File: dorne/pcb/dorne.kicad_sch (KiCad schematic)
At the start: 146 parts, among them J1 MJ-4PP-9, J2 OLED, J3 MJ-4PP-9, J4 OLED, SW1 SW_PUSH, SW10 SW_PUSH, SW11 SW_PUSH, SW12 SW_PUSH, SW13 SW_PUSH, SW14 SW_PUSH, SW15 SW_PUSH, SW16 SW_PUSH, SW17 SW_PUSH, SW18 SW_PUSH, SW19 SW_PUSH, SW2 SW_PUSH, SW20 SW_PUSH, SW21 SW_PUSH, SW22 SW_PUSH, SW23 SW_PUSH, SW24 SW_PUSH, SW25 SW_PUSH, SW26 SW_PUSH, SW27 SW_PUSH, SW28 SW_PUSH, SW29 SW_PUSH, SW3 SW_PUSH, SW30 SW_PUSH, SW31 SW_PUSH, SW32 SW_PUSH, SW33 SW_PUSH, SW34 SW_PUSH, SW35 SW_PUSH, SW36 SW_PUSH, SW37 SW_PUSH, SW38 SW_PUSH, SW39 SW_PUSH, SW4 SW_PUSH, SW40 SW_PUSH, SW41 SW_PUSH, SW42 SW_PUSH, SW5 SW_PUSH, SW6 SW_PUSH, SW7 SW_PUSH, SW8 SW_PUSH, SW9 SW_PUSH, U1 ProMicro, U2 ProMicro

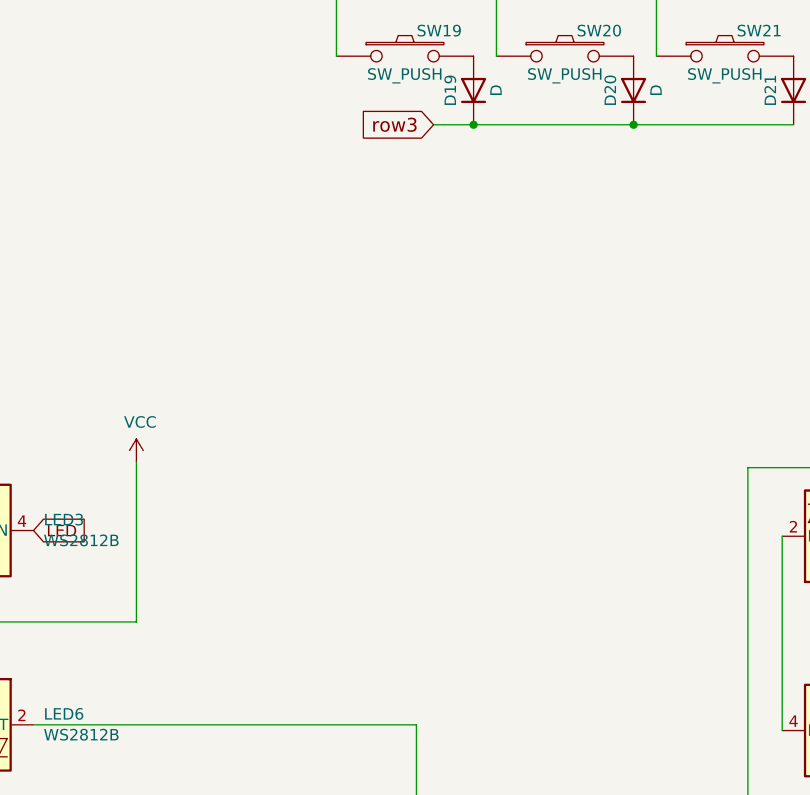
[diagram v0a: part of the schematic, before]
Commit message: Add Nice-Nano
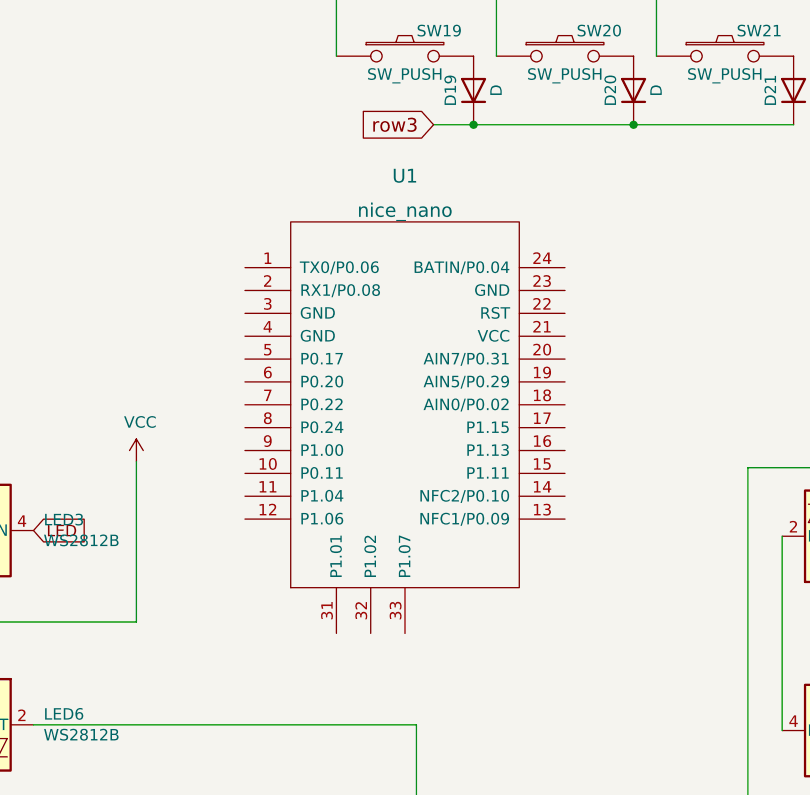
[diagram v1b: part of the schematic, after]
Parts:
- added U1: nice_nano, symbol nice:nice_nano
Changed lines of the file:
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@@
     (pin "1")
+  )
+  (symbol (lib_id "nice:nice_nano") (at 152.4 115.57 0) (unit 1)
+    (in_bom yes) (on_board yes) (fields_autoplaced)
+    (property "Reference" "U1" (id 0) (at 152.4 91.44 0)
+      (effects (font (size 1.524 1.524)))
+    )
+    (property "Value" "nice_nano" (id 1) (at 152.4 95.25 0)
+      (effects (font (size 1.524 1.524)))
+    )
+    (property "Footprint" "" (id 2) (at 179.07 179.07 90)
+      (effects (font (size 1.524 1.524)) hide)
+    )
+    (property "Datasheet" "" (id 3) (at 179.07 179.07 90)
+      (effects (font (size 1.524 1.524)) hide)
+    )
+    (pin "1")
+    (pin "10")
+    (pin "11")
+    (pin "12")
+    (pin "13")
+    (pin "14")
+    (pin "15")
+    (pin "16")
+    (pin "17")
+    (pin "18")
+    (pin "19")
+    (pin "2")
+    (pin "20")
+    (pin "21")
+    (pin "22")
+    (pin "23")
+    (pin "24")
+    (pin "3")
+    (pin "31")
+    (pin "32")
+    (pin "33")
+    (pin "4")
+    (pin "5")
+    (pin "6")
+    (pin "7")
+    (pin "8")
+    (pin "9")
   )
   (sheet_instances
@@
       (reference "U1") (unit 1) (value "ProMicro") (footprint "kbd:ProMicro_v3")
     )
+    (path "/2c564cbd-303f-4000-890a-52bc3be8e7ab"
+      (reference "U1") (unit 1) (value "nice_nano") (footprint "")
+    )
     (path "/00000000-0000-0000-0000-00005c25f857"

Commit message: RM LEDs
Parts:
- removed LED1, LED2, LED28, LED29, LED3, LED30, LED31, LED32, LED33, LED4, LED5, LED6: WS2812B, LED_SMD:LED_WS2812B_PLCC4_5.0x5.0mm_P3.2mm, symbol LED:WS2812B
- removed LED10, LED11, LED12, LED13, LED14, LED15, LED16, LED17, LED18, LED19, LED20, LED21, LED22, LED23, LED24, LED25, LED26, LED27, LED34, LED35, LED36, LED37, LED38, LED39, LED40, LED41, LED42, LED43, LED44, LED45, LED46, LED47, LED48, LED49, LED50, LED51, LED52, LED53, LED54, LED7, LED8, LED9: YS-SK6812MINI-E, kbd:YS-SK6812MINI-E, symbol kbd:YS-SK6812MINI-E
- removed U1: nice_nano, symbol nice:nice_nano
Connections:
- no-connect marks 14 -> 12

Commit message: cherry->choc
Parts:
- SW1, SW10, SW11, SW12, SW13, SW14, SW15, SW16, SW17, SW18, SW19, SW2, SW20, SW22, SW23, SW24, SW25, SW26, SW27, SW28, SW29, SW3, SW30, SW31, SW32, SW33, SW34, SW35, SW36, SW37, SW38, SW39, SW4, SW40, SW41, SW5, SW6, SW7, SW8, SW9: footprint kbd:CherryMX_Hotswap -> kbd:ChocV1_V2_Hotswap
- SW21, SW42: footprint kbd:CherryMX_Hotswap_1.5u -> kbd:ChocV1_V2_Hotswap_1.5u

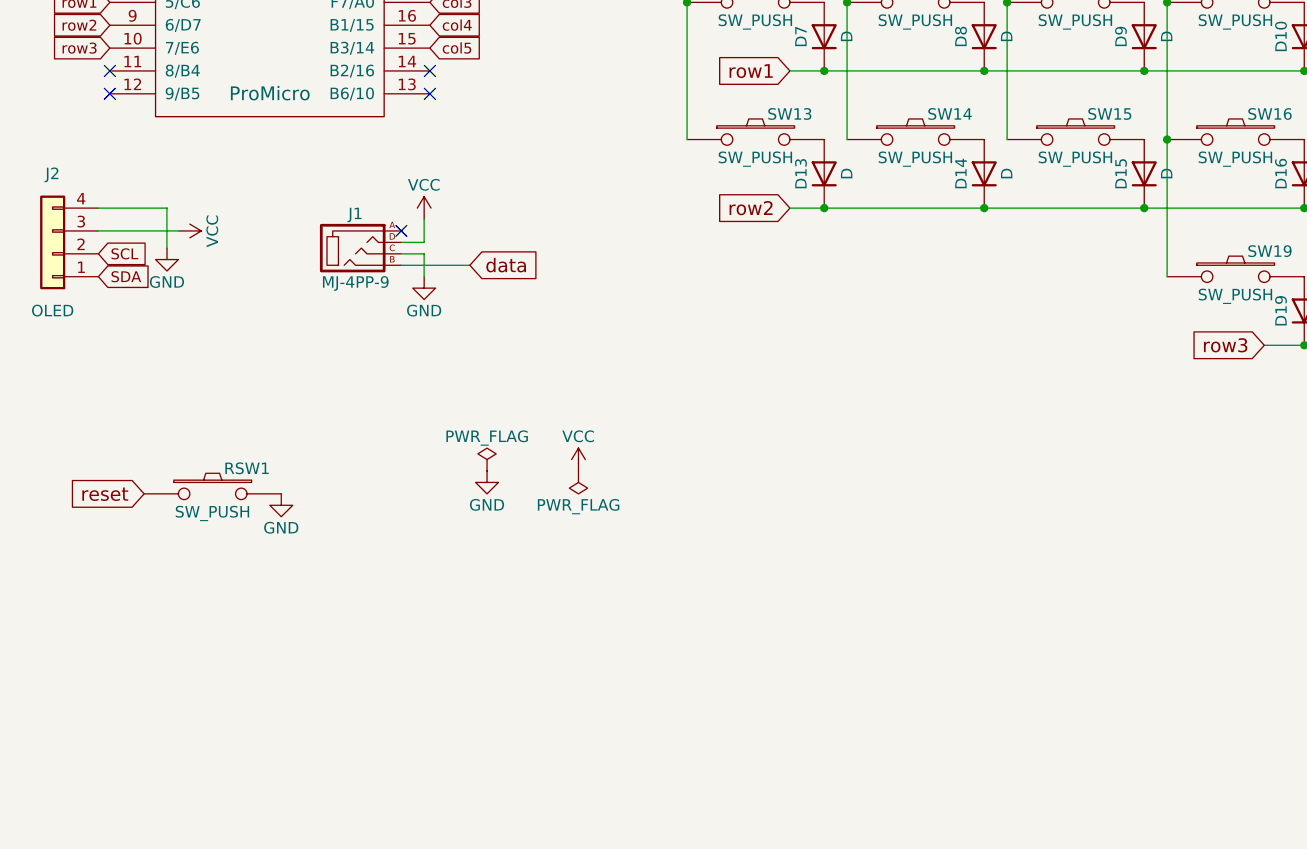
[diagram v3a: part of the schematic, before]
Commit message: Starting to integrate nice nano
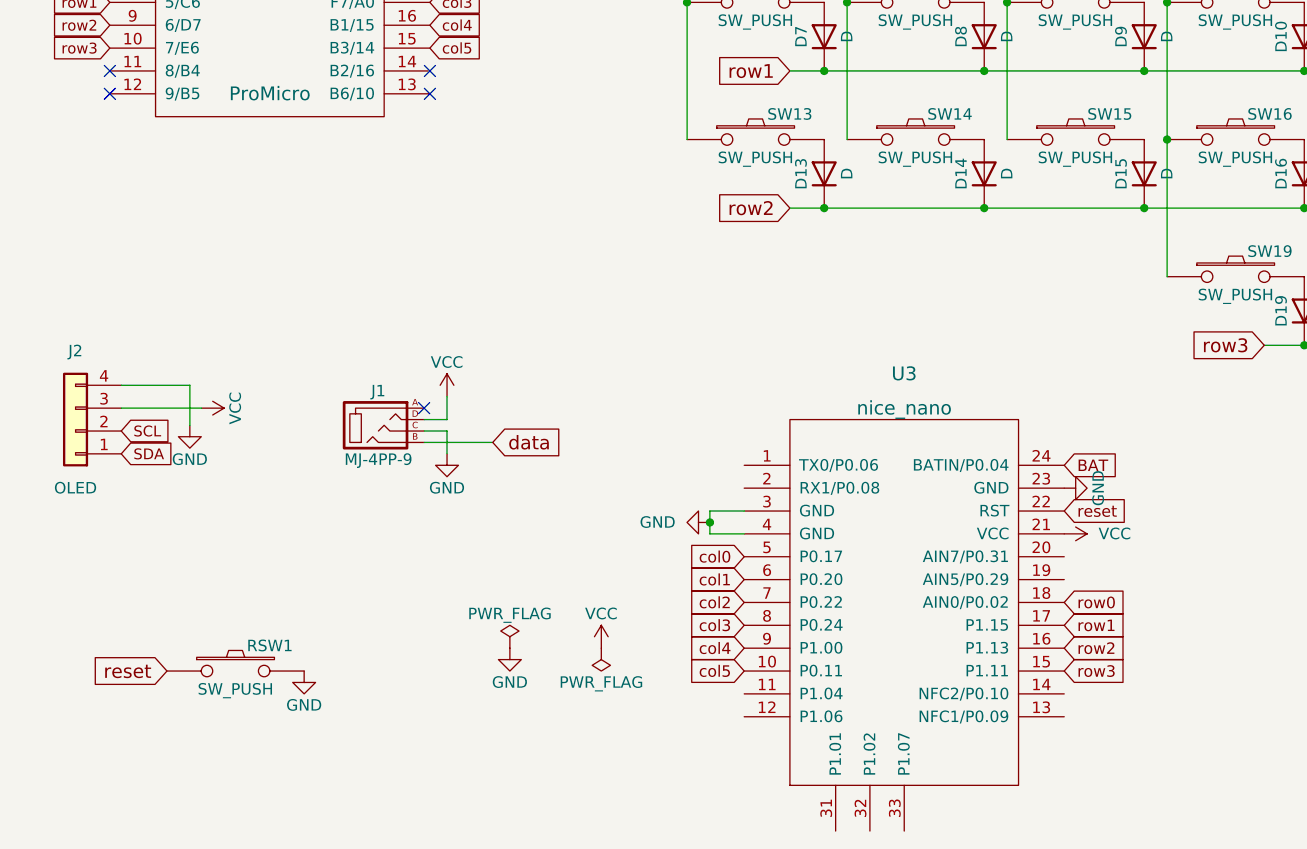
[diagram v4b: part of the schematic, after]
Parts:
- added U3: nice_nano, symbol nice:nice_nano
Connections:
- net GND: now also U3.23 (GND), U3.3 (GND), U3.4 (GND)
- net VCC: now also U3.21 (VCC)
- net col0: now also U3.5 (P0.17)
- net col1: now also U3.6 (P0.20)
- net col2: now also U3.7 (P0.22)
- net col3: now also U3.8 (P0.24)
- net col4: now also U3.9 (P1.00)
- net col5: now also U3.10 (P0.11)
- net reset: now also U3.22 (RST)
- net row0: now also U3.18 (AIN0/P0.02)
- net row1: now also U3.17 (P1.15)
- net row2: now also U3.16 (P1.13)
- net row3: now also U3.15 (P1.11)
- new net BAT: U3.24 (BATIN/P0.04)
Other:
- moved on the sheet: J1, J2, RSW1

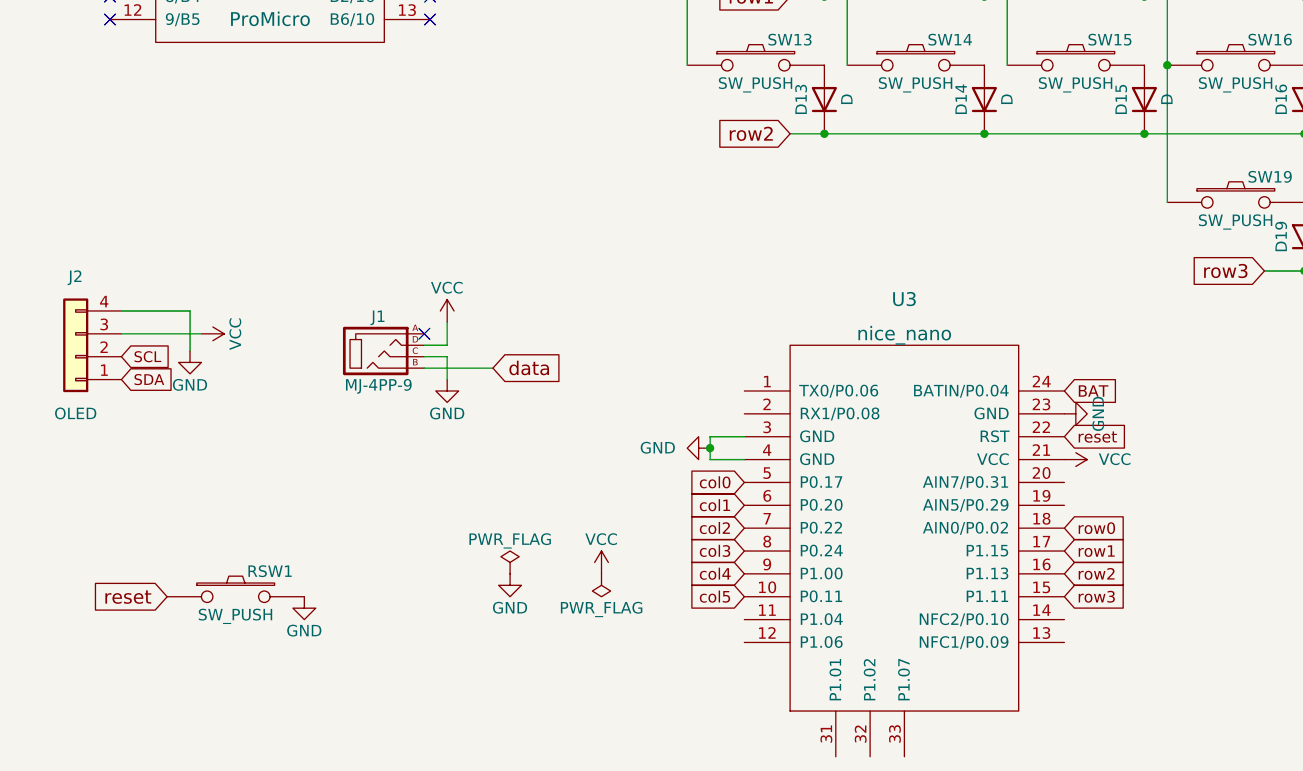
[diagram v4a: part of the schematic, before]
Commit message: Left half is routed better now
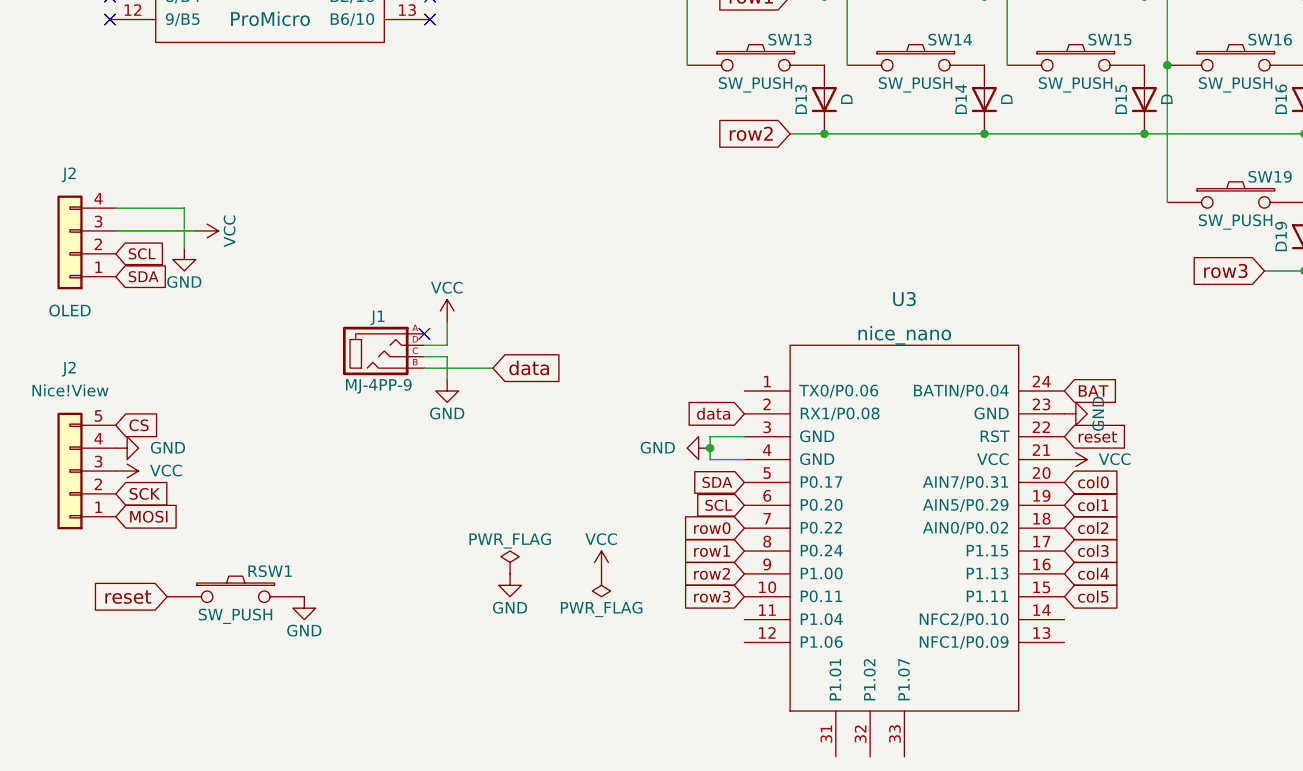
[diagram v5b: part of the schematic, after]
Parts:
- added J2: Nice!View, symbol Connector_Generic:Conn_01x05
- U3: footprint (none) -> nicenano:nice_nano
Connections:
- net GND: now also J2.4 (Pin_4)
- net SCL: now also U3.6 (P0.20)
- net SDA: now also U3.5 (P0.17)
- net VCC: now also J2.3 (Pin_3)
- net col0: now also U3.20 (AIN7/P0.31); no longer U3.5 (P0.17)
- net col1: now also U3.19 (AIN5/P0.29); no longer U3.6 (P0.20)
- net col2: now also U3.18 (AIN0/P0.02); no longer U3.7 (P0.22)
- net col3: now also U3.17 (P1.15); no longer U3.8 (P0.24)
- net col4: now also U3.16 (P1.13); no longer U3.9 (P1.00)
- net col5: now also U3.15 (P1.11); no longer U3.10 (P0.11)
- net data: now also U3.2 (RX1/P0.08)
- net row0: now also U3.7 (P0.22); no longer U3.18 (AIN0/P0.02)
- net row1: now also U3.8 (P0.24); no longer U3.17 (P1.15)
- net row2: now also U3.9 (P1.00); no longer U3.16 (P1.13)
- net row3: now also U3.10 (P0.11); no longer U3.15 (P1.11)
- new net CS: J2.5 (Pin_5)
- new net MOSI: J2.1 (Pin_1)
- new net SCK: J2.2 (Pin_2)
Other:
- moved on the sheet: J2

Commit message: Saving state
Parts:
- removed J2, J4: OLED, kbd:OLED_1side, symbol Connector_Generic:Conn_01x04
- removed J2: Nice!View, symbol Connector_Generic:Conn_01x05
- removed J3: MJ-4PP-9, kbd:MJ-4PP-9_1side, symbol kbd:MJ-4PP-9
- removed U1, U2: ProMicro, kbd:ProMicro_v3, symbol kbd:ProMicro
- added H0, H1: MountingHole_Pad, Connector_Pin:Pin_D1.0mm_L10.0mm, symbol Mechanical:MountingHole_Pad
- added J2: MJ-4PP-9, kbd:MJ-4PP-9_1side, symbol kbd:MJ-4PP-9
- added SW0: SW_SPDT, lib:ALPS-SSSS811101-0, symbol Switch:SW_SPDT
- added U4: nice_nano, nicenano:nice_nano, symbol nice:nice_nano
- RSW1, RSW2: footprint kbd:ResetSW_1side -> Button_Switch_SMD:SW_Push_SPST_NO_Alps_SKRK
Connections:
- net GND: now also H1.1
- net GNDA: now also J2.C, U4.23 (GND), U4.3 (GND), U4.4 (GND)
- net VDD: now also J2.D, U4.21 (VCC)
- net col0_r: now also U4.20 (AIN7/P0.31)
- net col1_r: now also U4.19 (AIN5/P0.29)
- net col2_r: now also U4.18 (AIN0/P0.02)
- net col3_r: now also U4.17 (P1.15)
- net col4_r: now also U4.16 (P1.13)
- net col5_r: now also U4.15 (P1.11)
- net data_r: now also J2.B, U4.2 (RX1/P0.08)
- net reset_r: now also U4.22 (RST)
- net row0_r: now also U4.7 (P0.22)
- net row1_r: now also U4.8 (P0.24)
- net row2_r: now also U4.9 (P1.00)
- net row3_r: now also U4.10 (P0.11)
- net BAT renamed bat_in
- net bat_in: now also SW0.1 (A)
- new net bat_in_r: U4.24 (BATIN/P0.04)
- new net bat_pos: H0.1, SW0.2 (B)
- no-connect marks 12 -> 2
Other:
- moved on the sheet: U3

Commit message: Finished everything??
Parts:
- added H2, H3: MountingHole_Pad, Connector_Pin:Pin_D1.0mm_L10.0mm, symbol Mechanical:MountingHole_Pad
- added PSW1: SW_SPDT, lib:ALPS-SSSS811101-0, symbol Switch:SW_SPDT
- renumbered SW0 to PSW0
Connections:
- net GNDA: now also H3.1
- net bat_in_r: now also PSW1.1 (A)
- new net bat_pos_r: H2.1, PSW1.2 (B)
- no-connect marks 2 -> 22
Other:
- moved on the sheet: D1, D10, D11, D12, D13, D14, D15, D16, D17, D18, D19, D2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
